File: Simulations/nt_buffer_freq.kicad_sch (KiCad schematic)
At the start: 20 parts, among them U1 MCP6021

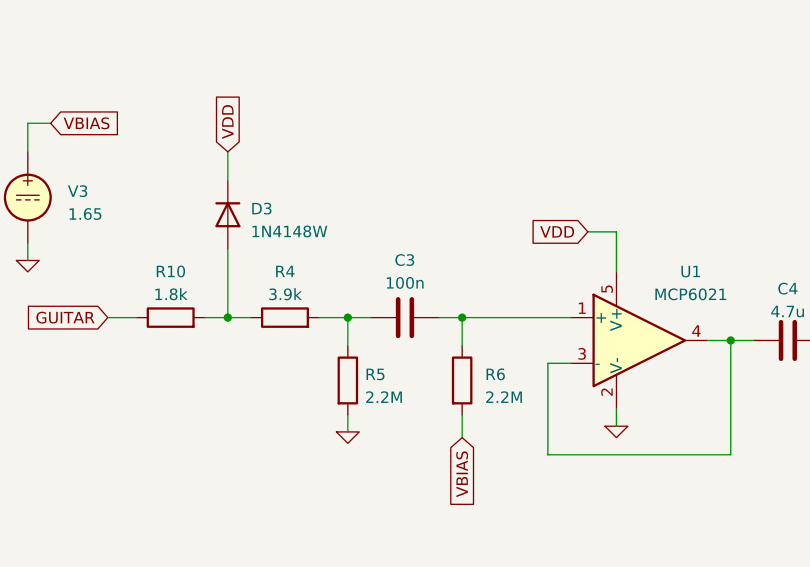
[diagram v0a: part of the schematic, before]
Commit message: change audio signal film cap to something more available
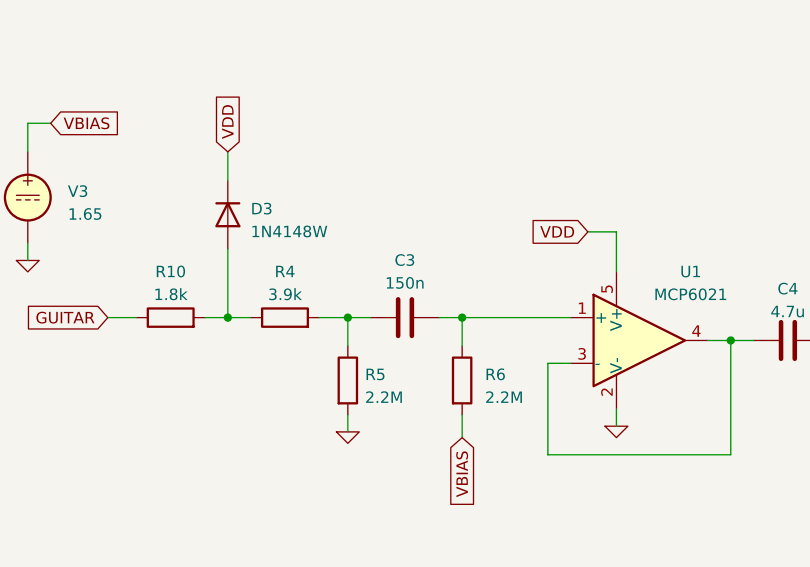
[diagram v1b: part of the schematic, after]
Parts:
- C3: value 100n -> 150n
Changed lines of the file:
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@@
       (effects (font (size 1.27 1.27)))
     )
-    (property "Value" "100n" (at 146.685 109.22 90)
+    (property "Value" "150n" (at 146.685 109.22 90)
       (effects (font (size 1.27 1.27)))
     )

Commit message: cleanup and lcsc part numbers
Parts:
- removed R5: 2.2M, symbol Device:R
- removed R8: 100, symbol Device:R
- C3: value 150n -> 100
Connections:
- net OUT: now also C4.2, R7.1
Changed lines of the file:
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@@
   (junction (at 133.35 74.93) (diameter 0) (color 0 0 0 0)
   )
-  (junction (at 140.335 113.03) (diameter 0) (color 0 0 0 0)
-  )
-  (wire (pts (xy 140.335 123.825) (xy 140.335 125.73))
-    (stroke (width 0) (type default))
-  )
   (wire (pts (xy 147.955 74.93) (xy 142.24 74.93))
     (stroke (width 0) (type default))
@@
     (stroke (width 0) (type default))
   )
-  (wire (pts (xy 206.375 115.57) (xy 208.915 115.57))
+  (wire (pts (xy 196.215 115.57) (xy 208.915 115.57))
     (stroke (width 0) (type default))
   )
@@
     (stroke (width 0) (type default))
   )
-  (wire (pts (xy 140.335 113.03) (xy 142.875 113.03))
-    (stroke (width 0) (type default))
-  )
   (wire (pts (xy 153.035 116.205) (xy 153.035 113.03))
     (stroke (width 0) (type default))
@@
     (stroke (width 0) (type default))
   )
-  (wire (pts (xy 140.335 113.03) (xy 140.335 116.205))
-    (stroke (width 0) (type default))
-  )
   (wire (pts (xy 133.35 57.15) (xy 142.24 57.15))
     (stroke (width 0) (type default))
@@
     (stroke (width 0) (type default))
   )
-  (wire (pts (xy 196.215 115.57) (xy 198.755 115.57))
-    (stroke (width 0) (type default))
-  )
   (wire (pts (xy 133.35 62.23) (xy 133.35 57.15))
     (stroke (width 0) (type default))
@@
     (stroke (width 0) (type default))
   )
-  (wire (pts (xy 137.16 113.03) (xy 140.335 113.03))
+  (wire (pts (xy 137.16 113.03) (xy 142.875 113.03))
     (stroke (width 0) (type default))
   )
@@
     )
   )
-  (symbol (lib_id "Device:R") (at 140.335 120.015 0) (unit 1)
-    (in_bom yes) (on_board yes) (dnp no) (fields_autoplaced)
-    (property "Reference" "R5" (at 142.24 119.38 0)
-      (effects (font (size 1.27 1.27)) (justify left))
-    )
-    (property "Value" "2.2M" (at 142.24 121.92 0)
-      (effects (font (size 1.27 1.27)) (justify left))
-    )
-    (property "Footprint" "" (at 138.557 120.015 90)
-      (effects (font (size 1.27 1.27)) hide)
-    )
-    (property "Datasheet" "~" (at 140.335 120.015 0)
-      (effects (font (size 1.27 1.27)) hide)
-    )
-    (pin "1")
-    (pin "2")
-    (instances
-      (project "nt_buffer_freq"
-        (path "/ea4fc8d5-926a-4e1e-b9cd-45e6fdca0bc8"
-          (reference "R5") (unit 1)
-        )
-      )
-    )
-  )
   (symbol (lib_id "Device:R") (at 120.65 113.03 90) (unit 1)
     (in_bom yes) (on_board yes) (dnp no) (fields_autoplaced)
@@
         (path "/ea4fc8d5-926a-4e1e-b9cd-45e6fdca0bc8"
           (reference "R10") (unit 1)
-        )
-      )
-    )
-  )
-  (symbol (lib_id "Simulation_SPICE:0") (at 140.335 125.73 0) (unit 1)
-    (in_bom yes) (on_board yes) (dnp no) (fields_autoplaced)
-    (property "Reference" "#GND05" (at 140.335 128.27 0)
-      (effects (font (size 1.27 1.27)) hide)
-    )
-    (property "Value" "0" (at 140.335 125.095 0)
-      (effects (font (size 1.27 1.27)) hide)
-    )
-    (property "Footprint" "" (at 140.335 125.73 0)
-      (effects (font (size 1.27 1.27)) hide)
-    )
-    (property "Datasheet" "~" (at 140.335 125.73 0)
-      (effects (font (size 1.27 1.27)) hide)
-    )
-    (pin "1")
-    (instances
-      (project "nt_buffer_freq"
-        (path "/ea4fc8d5-926a-4e1e-b9cd-45e6fdca0bc8"
-          (reference "#GND05") (unit 1)
         )
       )
@@
     )
   )
-  (symbol (lib_id "Device:R") (at 202.565 115.57 90) (unit 1)
-    (in_bom yes) (on_board yes) (dnp no) (fields_autoplaced)
-    (property "Reference" "R8" (at 202.565 111.125 90)
-      (effects (font (size 1.27 1.27)))
-    )
-    (property "Value" "100" (at 202.565 113.665 90)
-      (effects (font (size 1.27 1.27)))
-    )
-    (property "Footprint" "" (at 202.565 117.348 90)
-      (effects (font (size 1.27 1.27)) hide)
-    )
-    (property "Datasheet" "~" (at 202.565 115.57 0)
-      (effects (font (size 1.27 1.27)) hide)
-    )
-    (pin "1")
-    (pin "2")
-    (instances
-      (project "nt_buffer_freq"
-        (path "/ea4fc8d5-926a-4e1e-b9cd-45e6fdca0bc8"
-          (reference "R8") (unit 1)
-        )
-      )
-    )
-  )
   (symbol (lib_id "Simulation_SPICE:0") (at 196.215 128.27 0) (unit 1)
     (in_bom yes) (on_board yes) (dnp no) (fields_autoplaced)
@@
       (effects (font (size 1.27 1.27)))
     )
-    (property "Value" "150n" (at 146.685 109.22 90)
-      (effects (font (size 1.27 1.27)))
-    )
+    (property "Value" "100" (at 146.685 109.22 90)
+      (effects (font (size 1.27 1.27)))
+    )
